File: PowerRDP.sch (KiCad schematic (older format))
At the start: 12 parts, among them J1 Conn_01x02_Male, J2 Conn_01x02_Male, J3 Conn_01x02_Male, J4 Conn_01x02_Male, J5 Conn_01x02_Male, J6 Conn_01x02_Male, J7 Conn_01x02_Male, J8 Conn_01x02_Male, J9 Conn_01x03_Male, U1 DPBW06F, U2 KA378R12C, U3 AZ1117-3.3

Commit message: create PCB layout and GERBERs
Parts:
- U1: footprint Package_SIP:SIP-8_19x3mm_P2.54mm -> RDP-Power:SIP-8_19x3mm_P2.54mm
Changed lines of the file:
@@
 EESchema Schematic File Version 4
+LIBS:PowerRDP-cache
 EELAYER 26 0
 EELAYER END
@@
 F 0 "U1" H 3450 1775 50  0000 C CNN
 F 1 "DPBW06F" H 3450 1684 50  0000 C CNN
-F 2 "Package_SIP:SIP-8_19x3mm_P2.54mm" H 3200 1650 50  0001 C CNN
+F 2 "RDP-Power:SIP-8_19x3mm_P2.54mm" H 3200 1650 50  0001 C CNN
 F 3 "" H 3200 1650 50  0001 C CNN
 	1    3450 1400

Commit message: remove old +/-15V add new (kicad files broken)
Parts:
- removed U1: DPBW06F, RDP-Power:SIP-8_19x3mm_P2.54mm, symbol RDP_Converter_DCDC:DPBW06F
- added U4: TMR_1-1223, Converter_DCDC:Converter_DCDC_TRACO_TMR-1-xxxx_Dual_THT, symbol Regulator_Switching:TMR_1-1223
- U3: value AZ1117-3.3 -> AZ1117CH-3.3
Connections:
- wire segments 23 -> 24
- no-connect marks 3 -> 1
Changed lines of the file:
@@
 	1200 800  1250 800
-$Comp
-L RDP_Converter_DCDC:DPBW06F U1
-U 1 1 5B9C65C7
-P 3450 1400
-F 0 "U1" H 3450 1775 50  0000 C CNN
-F 1 "DPBW06F" H 3450 1684 50  0000 C CNN
-F 2 "RDP-Power:SIP-8_19x3mm_P2.54mm" H 3200 1650 50  0001 C CNN
-F 3 "" H 3200 1650 50  0001 C CNN
-	1    3450 1400
-	1    0    0    -1
-$EndComp
-Wire Wire Line
-	2900 1350 3100 1350
-Wire Wire Line
-	2900 1250 3100 1250
-Wire Wire Line
-	3800 1350 4000 1350
-Wire Wire Line
-	3800 1550 4000 1550
-$Comp
-L power:+BATT #PWR0102
-U 1 1 5B9C7BFF
-P 2900 1350
-F 0 "#PWR0102" H 2900 1200 50  0001 C CNN
-F 1 "+BATT" V 2915 1477 50  0000 L CNN
-F 2 "" H 2900 1350 50  0001 C CNN
-F 3 "" H 2900 1350 50  0001 C CNN
-	1    2900 1350
-	0    -1   -1   0
-$EndComp
-NoConn ~ 3100 1450
-Text Label 4000 1350 2    50   ~ 0
-+15V
-Text Label 4000 1550 2    50   ~ 0
--15V
-NoConn ~ 3800 1450
 $Comp
 L Regulator_Linear:KA378R12C U2
@@
 P 7300 1200
 F 0 "U3" H 7300 1442 50  0000 C CNN
-F 1 "AZ1117-3.3" H 7300 1351 50  0000 C CNN
+F 1 "AZ1117CH-3.3" H 7300 1351 50  0000 C CNN
 F 2 "Package_TO_SOT_SMD:SOT-223" H 7300 1450 50  0001 C CIN
 F 3 "https://www.diodes.com/assets/Datasheets/AZ1117.pdf" H 7300 1200 50  0001 C CNN
@@
 Wire Wire Line
 	1250 2700 1300 2700
-$Comp
-L power:GND #PWR0103
-U 1 1 5B9D9D21
-P 2900 1250
-F 0 "#PWR0103" H 2900 1000 50  0001 C CNN
-F 1 "GND" H 2905 1077 50  0000 C CNN
-F 2 "" H 2900 1250 50  0001 C CNN
-F 3 "" H 2900 1250 50  0001 C CNN
-	1    2900 1250
-	-1   0    0    1
-$EndComp
 Wire Wire Line
 	1250 800  1250 600
@@
 	0    -1   -1   0
 $EndComp
+$Comp
+L Regulator_Switching:TMR_1-1223 U4
+U 1 1 5BBD6B92
+P 3350 1400
+F 0 "U4" H 3350 1867 50  0000 C CNN
+F 1 "TMR_1-1223" H 3350 1776 50  0000 C CNN
+F 2 "Converter_DCDC:Converter_DCDC_TRACO_TMR-1-xxxx_Dual_THT" H 3350 1050 50  0001 C CNN
+F 3 "http://assets.tracopower.com/TMR1/documents/tmr1-datasheet.pdf" H 3350 900 50  0001 C CNN
+	1    3350 1400
+	1    0    0    -1
+$EndComp
+Wire Wire Line
+	4050 1200 3850 1200
+Wire Wire Line
+	4050 1600 3850 1600
+Wire Wire Line
+	4050 1400 3850 1400
+Wire Wire Line
+	2650 1200 2850 1200
+Wire Wire Line
+	2650 1600 2850 1600
 $EndSCHEMATC

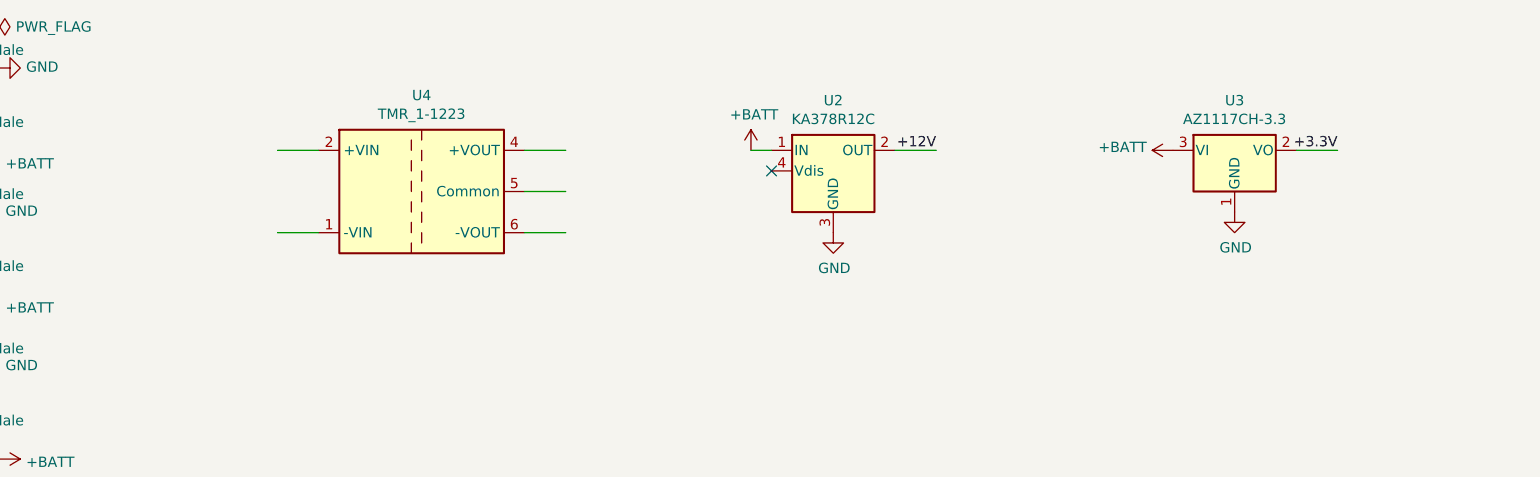
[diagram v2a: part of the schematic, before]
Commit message: Add power filtering to all regulators, correct +/-15V regulator
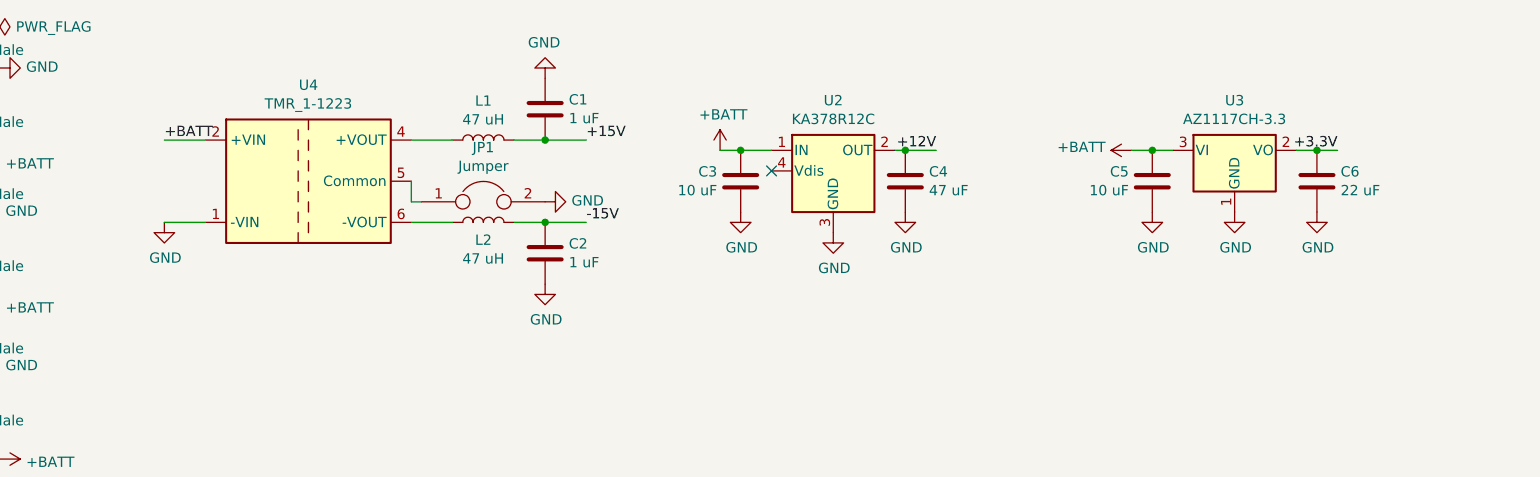
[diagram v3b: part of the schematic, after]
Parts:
- added C1, C2: 1 uF, Capacitor_SMD:C_0805_2012Metric_Pad1.15x1.40mm_HandSolder, symbol Device:C
- added C3, C5: 10 uF, Capacitor_SMD:C_0805_2012Metric_Pad1.15x1.40mm_HandSolder, symbol Device:C
- added C4: 47 uF, Capacitor_SMD:C_0805_2012Metric_Pad1.15x1.40mm_HandSolder, symbol Device:C
- added C6: 22 uF, Capacitor_SMD:C_0805_2012Metric_Pad1.15x1.40mm_HandSolder, symbol Device:C
- added JP1: Jumper, Jumper:SolderJumper-2_P1.3mm_Open_Pad1.0x1.5mm, symbol Device:Jumper
- added L1, L2: 47 uH, RDP-Power:Murata 8200, symbol Device:L
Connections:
- wire segments 24 -> 34
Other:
- moved on the sheet: U4

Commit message: Correct 15V regulator footprint, add potentiometer for socket gain control
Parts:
- added RV1: R_POT, Potentiometer_SMD:Potentiometer_Bourns_3214W_Vertical, symbol Device:R_POT
- J9: footprint Connector_Molex:Molex_KK-254_AE-6410-03A_1x03_P2.54mm_Vertical -> Connector_Molex:Molex_KK-254_AE-6410-05A_1x05_P2.54mm_Vertical; symbol Connector:Conn_01x03_Male -> Connector:Conn_01x05_Male
- L1, L2: footprint RDP-Power:Murata 8200 -> rdplibs:Murata 8200
- U4: value TMR_1-1223 -> MEA1D1515SC; symbol Regulator_Switching:TMR_1-1223 -> Regulator_Switching:MEA1
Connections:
- net +15V: now also C2.1, L2.2; no longer C1.1, L1.2
- net +BATT: now also U4.1 (+VIN); no longer U4.2 (+VIN)
- net -15V: now also C1.1, L1.2; no longer C2.1, L2.2
- net GND: now also U4.2 (-VIN), RV1.3; no longer U4.1 (-VIN)
- new net C_in: J9.4 (Pin_4), RV1.1
- new net C_out: J9.5 (Pin_5), RV1.2
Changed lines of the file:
@@
 $EndComp
 $Comp
-L Connector:Conn_01x03_Male J9
+L Connector:Conn_01x05_Male J9
 U 1 1 5B9DC0D0
-P 9150 1600
-F 0 "J9" H 9256 1878 50  0000 C CNN
-F 1 "Conn_01x03_Male" H 9256 1787 50  0000 C CNN
-F 2 "Connector_Molex:Molex_KK-254_AE-6410-03A_1x03_P2.54mm_Vertical" H 9150 1600 50  0001 C CNN
-F 3 "~" H 9150 1600 50  0001 C CNN
-	1    9150 1600
+P 9150 1700
+F 0 "J9" H 9150 2050 50  0000 C CNN
+F 1 "Conn_01x03_Male" H 9150 1950 50  0000 C CNN
+F 2 "Connector_Molex:Molex_KK-254_AE-6410-05A_1x05_P2.54mm_Vertical" H 9150 1700 50  0001 C CNN
+F 3 "~" H 9150 1700 50  0001 C CNN
+	1    9150 1700
 	1    0    0    -1
 $EndComp
@@
 $EndComp
 $Comp
-L Regulator_Switching:TMR_1-1223 U4
+L Regulator_Switching:MEA1 U4
 U 1 1 5BBD6B92
 P 2800 1350
 F 0 "U4" H 2800 1817 50  0000 C CNN
-F 1 "TMR_1-1223" H 2800 1726 50  0000 C CNN
+F 1 "MEA1D1515SC" H 2800 1726 50  0000 C CNN
 F 2 "Converter_DCDC:Converter_DCDC_TRACO_TMR-1-xxxx_Dual_THT" H 2800 1000 50  0001 C CNN
 F 3 "http://assets.tracopower.com/TMR1/documents/tmr1-datasheet.pdf" H 2800 850 50  0001 C CNN
@@
 F 0 "L1" V 3840 1150 50  0000 C CNN
 F 1 "47 uH" V 3749 1150 50  0000 C CNN
-F 2 "RDP-Power:Murata 8200" H 3650 1150 50  0001 C CNN
+F 2 "rdplibs:Murata 8200" H 3650 1150 50  0001 C CNN
 F 3 "~" H 3650 1150 50  0001 C CNN
 	1    3650 1150
@@
 F 0 "L2" V 3564 1550 50  0000 C CNN
 F 1 "47 uH" V 3473 1550 50  0000 C CNN
-F 2 "RDP-Power:Murata 8200" H 3650 1550 50  0001 C CNN
+F 2 "rdplibs:Murata 8200" H 3650 1550 50  0001 C CNN
 F 3 "~" H 3650 1550 50  0001 C CNN
 	1    3650 1550
@@
 Connection ~ 3950 1550
 Text Label 4150 1150 0    50   ~ 0
+-15V
+Text Label 4150 1550 0    50   ~ 0
 +15V
-Text Label 4150 1550 0    50   ~ 0
--15V
-Text Label 2100 1150 0    50   ~ 0
-+BATT
-$Comp
-L power:GND #PWR0117
-U 1 1 5BC66B8E
-P 2100 1550
-F 0 "#PWR0117" H 2100 1300 50  0001 C CNN
-F 1 "GND" H 2105 1377 50  0000 C CNN
-F 2 "" H 2100 1550 50  0001 C CNN
-F 3 "" H 2100 1550 50  0001 C CNN
-	1    2100 1550
-	1    0    0    -1
-$EndComp
 Wire Wire Line
 	4800 1200 4900 1200
@@
 	1    0    0    -1
 $EndComp
+$Comp
+L power:GND #PWR0117
+U 1 1 5C38679E
+P 2100 1150
+F 0 "#PWR0117" H 2100 900 50  0001 C CNN
+F 1 "GND" H 2105 977 50  0000 C CNN
+F 2 "" H 2100 1150 50  0001 C CNN
+F 3 "" H 2100 1150 50  0001 C CNN
+	1    2100 1150
+	-1   0    0    1
+$EndComp
+Text Label 2100 1550 0    50   ~ 0
++BATT
+Wire Wire Line
+	9350 1800 9550 1800
+Wire Wire Line
+	9350 1900 9550 1900
+Text Label 9550 1800 2    50   ~ 0
+C_in
+Text Label 9550 1900 2    50   ~ 0
+C_out
+$Comp
+L Device:R_POT RV1
+U 1 1 5C38925B
+P 8600 2250
+F 0 "RV1" V 8393 2250 50  0000 C CNN
+F 1 "R_POT" V 8484 2250 50  0000 C CNN
+F 2 "Potentiometer_SMD:Potentiometer_Bourns_3214W_Vertical" H 8600 2250 50  0001 C CNN
+F 3 "~" H 8600 2250 50  0001 C CNN
+	1    8600 2250
+	0    1    1    0
+$EndComp
+Wire Wire Line
+	8900 2250 8750 2250
+Text Label 8900 2250 2    50   ~ 0
+C_in
+Text Label 8650 2600 0    50   ~ 0
+C_out
+Wire Wire Line
+	8150 2250 8450 2250
+Wire Wire Line
+	8600 2400 8600 2600
+Wire Wire Line
+	8600 2600 8650 2600
+$Comp
+L power:GND #PWR0122
+U 1 1 5C38E9B8
+P 8150 2250
+F 0 "#PWR0122" H 8150 2000 50  0001 C CNN
+F 1 "GND" H 8155 2077 50  0000 C CNN
+F 2 "" H 8150 2250 50  0001 C CNN
+F 3 "" H 8150 2250 50  0001 C CNN
+	1    8150 2250
+	1    0    0    -1
+$EndComp

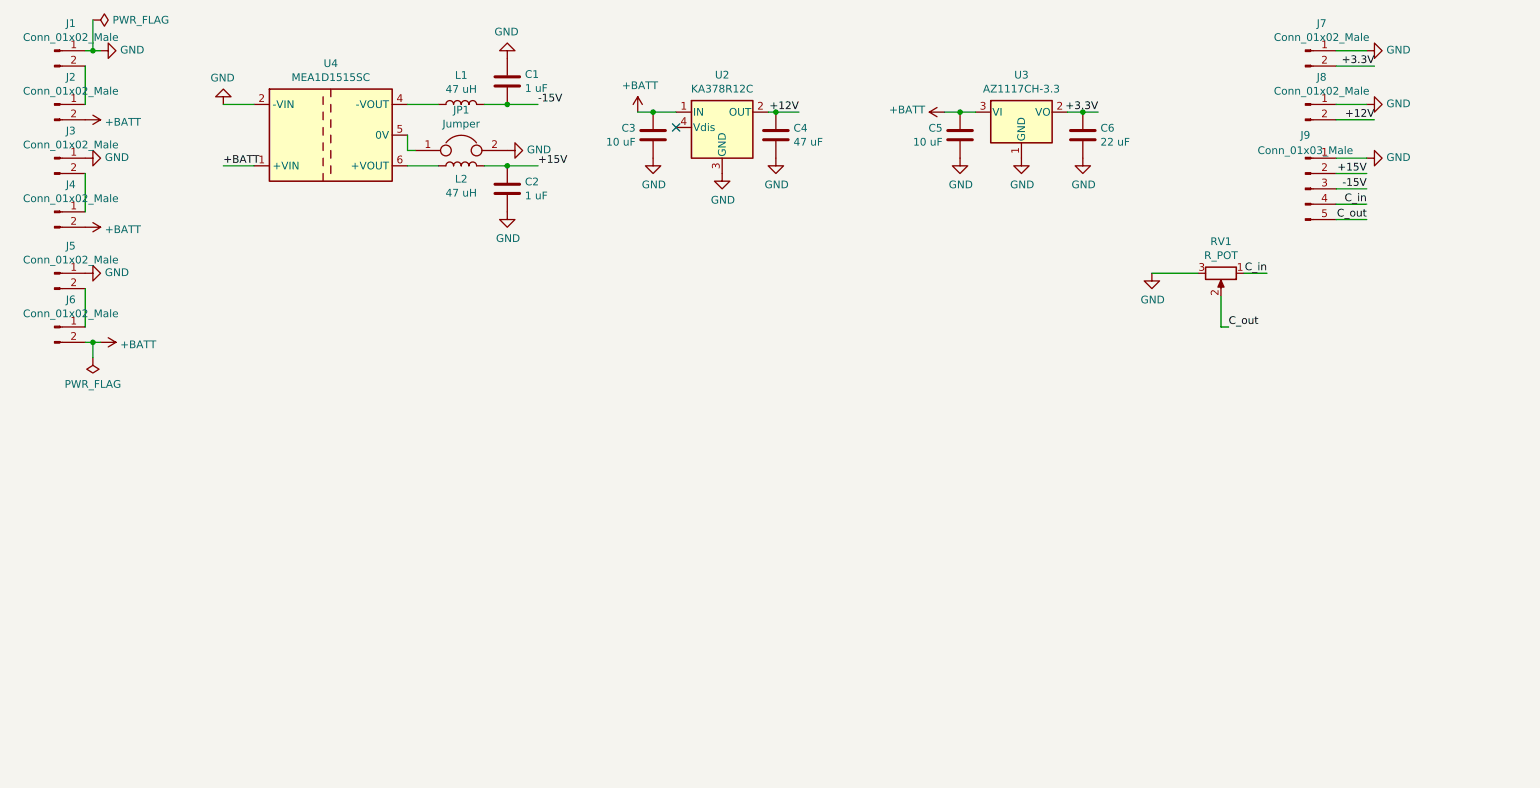
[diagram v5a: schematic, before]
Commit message: Fix 15V regulator, add blinking FAA LEDs
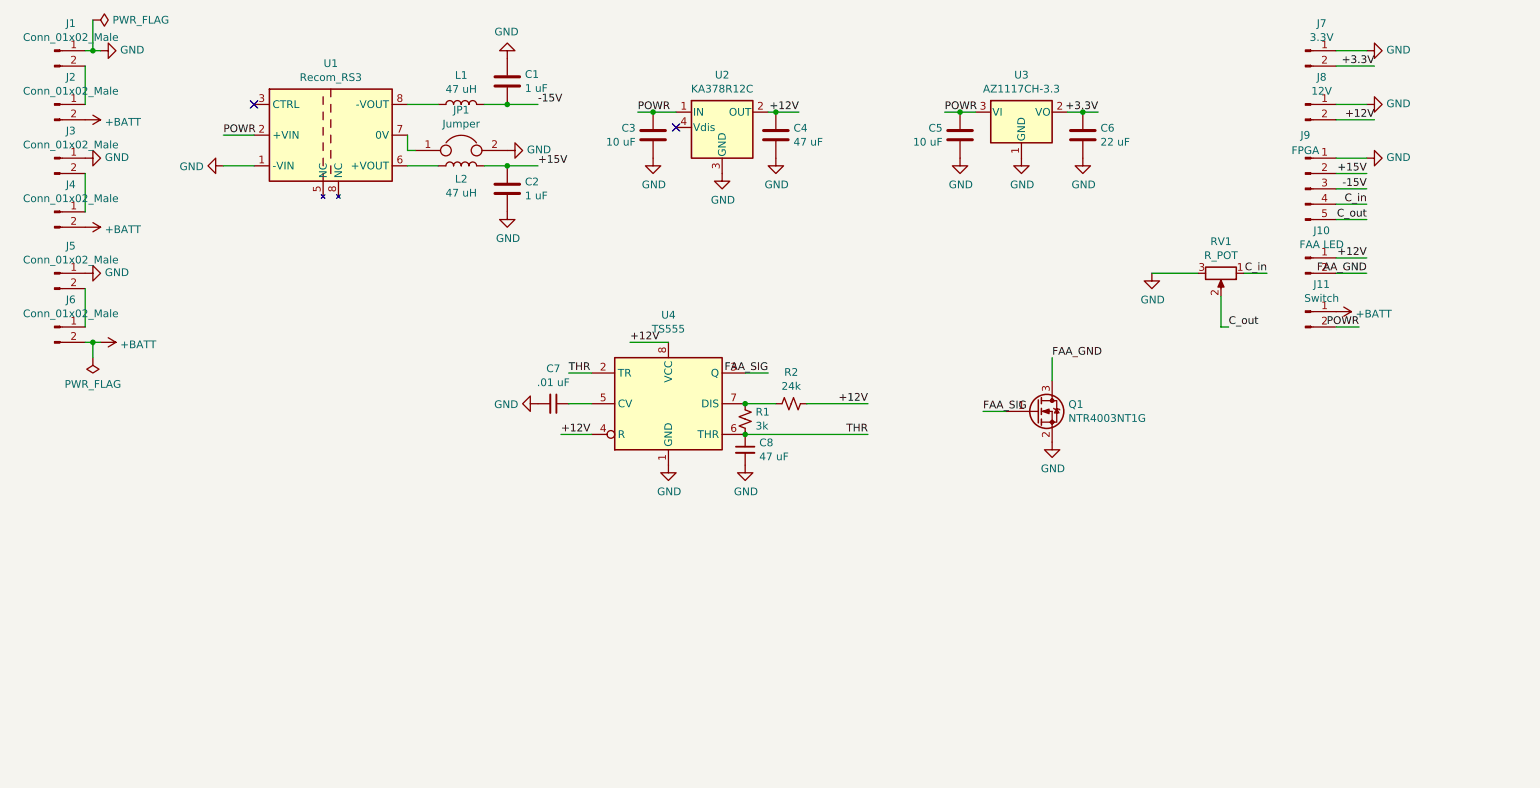
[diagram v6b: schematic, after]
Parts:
- removed U4: MEA1D1515SC, Converter_DCDC:Converter_DCDC_TRACO_TMR-1-xxxx_Dual_THT, symbol Regulator_Switching:MEA1
- added C7: .01 uF, Capacitor_SMD:C_0805_2012Metric_Pad1.15x1.40mm_HandSolder, symbol Device:C_Small
- added C8: 47 uF, Capacitor_SMD:C_0805_2012Metric_Pad1.15x1.40mm_HandSolder, symbol Device:C_Small
- added J10: FAA LED, Connector_Molex:Molex_KK-254_AE-6410-02A_1x02_P2.54mm_Vertical, symbol Connector:Conn_01x02_Male
- added J11: Switch, Connector_Molex:Molex_KK-254_AE-6410-02A_1x02_P2.54mm_Vertical, symbol Connector:Conn_01x02_Male
- added Q1: NTR4003NT1G, Package_TO_SOT_SMD:TSOT-23_HandSoldering, symbol Device:Q_NMOS_GSD
- added R1: 3k, Resistor_SMD:R_0805_2012Metric_Pad1.15x1.40mm_HandSolder, symbol Device:R_Small_US
- added R2: 24k, Resistor_SMD:R_0805_2012Metric_Pad1.15x1.40mm_HandSolder, symbol Device:R_Small_US
- added U1: Recom_RS3, PowerRDP:Recom_RS3, symbol PowerRDP-rescue:Recom_RS3-PowerRDP-cache
- added U4: TS555, Package_SO:SOIC-8_3.9x4.9mm_P1.27mm, symbol Timer:LM555
- J7: value Conn_01x02_Male -> 3.3V
- J8: value Conn_01x02_Male -> 12V
- J9: value Conn_01x03_Male -> FPGA
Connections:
- net +12V: now also J10.1 (Pin_1), R2.1, U4.4 (R), U4.8 (VCC)
- net +BATT: now also J11.1 (Pin_1); no longer C3.2, C5.1, U2.1 (IN), U3.3 (VI)
- net GND: now also C7.2, C8.2, Q1.2 (S), U1.1 (-VIN), U4.1 (GND)
- net at L1.1: now also U1.8 (NC)
- net at JP1.1: now also U1.7 (0V)
- net at L2.1: now also U1.6 (+VOUT)
- new net: C7.1, U4.5 (CV)
- new net: R1.1, R2.2, U4.7 (DIS)
- new net FAA_GND: J10.2 (Pin_2), Q1.3 (D)
- new net FAA_SIG: Q1.1 (G), U4.3 (Q)
- new net POWR: C3.2, C5.1, J11.2 (Pin_2), U1.2 (+VIN), U2.1 (IN), U3.3 (VI)
- new net THR: C8.1, R1.2, U4.2 (TR), U4.6 (THR)
- no-connect marks 1 -> 2

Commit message: Remake power board with updated single-output regulators. PCB entirely redesigned
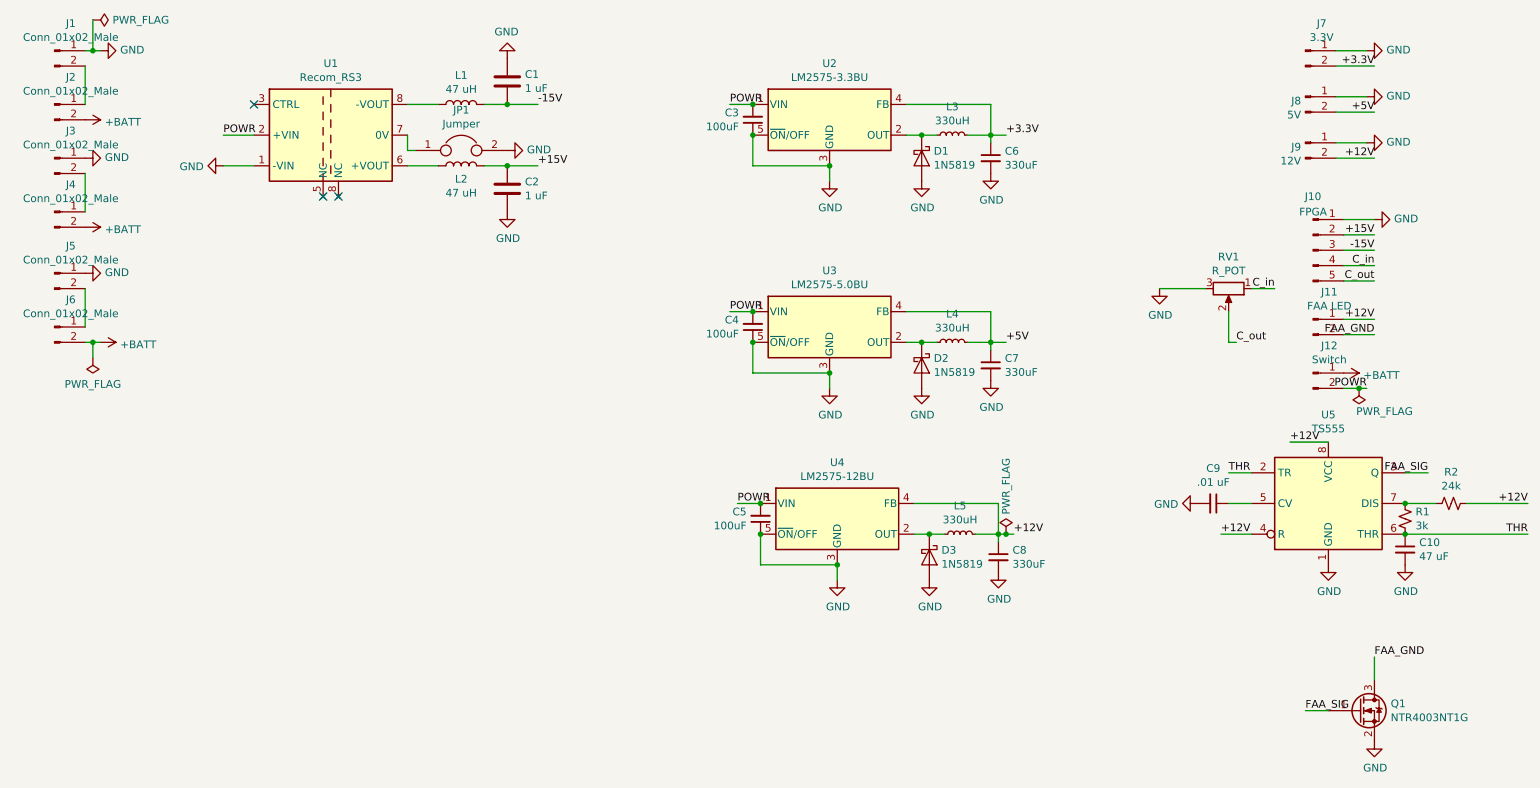
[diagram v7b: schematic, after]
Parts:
- removed C3, C5: 10 uF, Capacitor_SMD:C_0805_2012Metric_Pad1.15x1.40mm_HandSolder, symbol Device:C
- removed C4: 47 uF, Capacitor_SMD:C_0805_2012Metric_Pad1.15x1.40mm_HandSolder, symbol Device:C
- removed C6: 22 uF, Capacitor_SMD:C_0805_2012Metric_Pad1.15x1.40mm_HandSolder, symbol Device:C
- removed U2: KA378R12C, Package_TO_SOT_THT:TO-220-4_Vertical, symbol Regulator_Linear:KA378R12C
- removed U3: AZ1117CH-3.3, Package_TO_SOT_SMD:SOT-223, symbol Regulator_Linear:AZ1117-3.3
- added C3, C4, C5: 100uF, Capacitor_SMD:C_0805_2012Metric_Pad1.15x1.40mm_HandSolder, symbol Device:C_Small
- added C6, C7, C8: 330uF, Capacitor_SMD:C_0805_2012Metric_Pad1.15x1.40mm_HandSolder, symbol Device:C_Small
- added D1, D2, D3: 1N5819, Diode_SMD:D_0805_2012Metric_Pad1.15x1.40mm_HandSolder, symbol Device:D_Schottky
- added J8: 5V, Connector_Molex:Molex_KK-254_AE-6410-02A_1x02_P2.54mm_Vertical, symbol Connector:Conn_01x02_Male
- added L3, L4, L5: 330uH, Inductor_SMD:L_0805_2012Metric_Pad1.15x1.40mm_HandSolder, symbol Device:L_Small
- added U2: LM2575-3.3BU, Package_TO_SOT_SMD:TO-263-5_TabPin3, symbol Regulator_Switching:LM2575-3.3BU
- added U3: LM2575-5.0BU, Package_TO_SOT_SMD:TO-263-5_TabPin3, symbol Regulator_Switching:LM2575-5.0BU
- added U4: LM2575-12BU, Package_TO_SOT_SMD:TO-263-5_TabPin3, symbol Regulator_Switching:LM2575-12BU
- renumbered C8 to C10, C7 to C9, J9 to J10, J10 to J11, J11 to J12, J8 to J9, U4 to U5
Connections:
- net +12V: now also C8.1, L5.2, U4.4 (FB)
- net +3.3V: now also C6.1, L3.2, U2.4 (FB)
- net GND: now also C3.1, C4.1, C5.1, C6.2, C7.2, C8.2, D1.2 (A), D2.2 (A), D3.2 (A), J8.1 (Pin_1), U2.3 (GND), U2.5 (~ON~/OFF), U3.3 (GND), U3.5 (~ON~/OFF), U4.3 (GND), U4.5 (~ON~/OFF)
- net POWR: now also C3.2, C4.2, C5.2, U2.1 (VIN), U3.1 (VIN), U4.1 (VIN)
- new net: D1.1 (K), L3.1, U2.2 (OUT)
- new net: D2.1 (K), L4.1, U3.2 (OUT)
- new net: D3.1 (K), L5.1, U4.2 (OUT)
- new net +5V: C7.1, J8.2 (Pin_2), L4.2, U3.4 (FB)
- no-connect marks 2 -> 3
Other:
- moved on the sheet: C10, C9, J10, J11, J12, J9, Q1, R1, R2, RV1, U5
